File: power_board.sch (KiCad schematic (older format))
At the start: 18 parts, among them J1 STANDBY SWITCH, J2 TRANSFORMER IN, J3 BIAS OUT, J4 HEATER

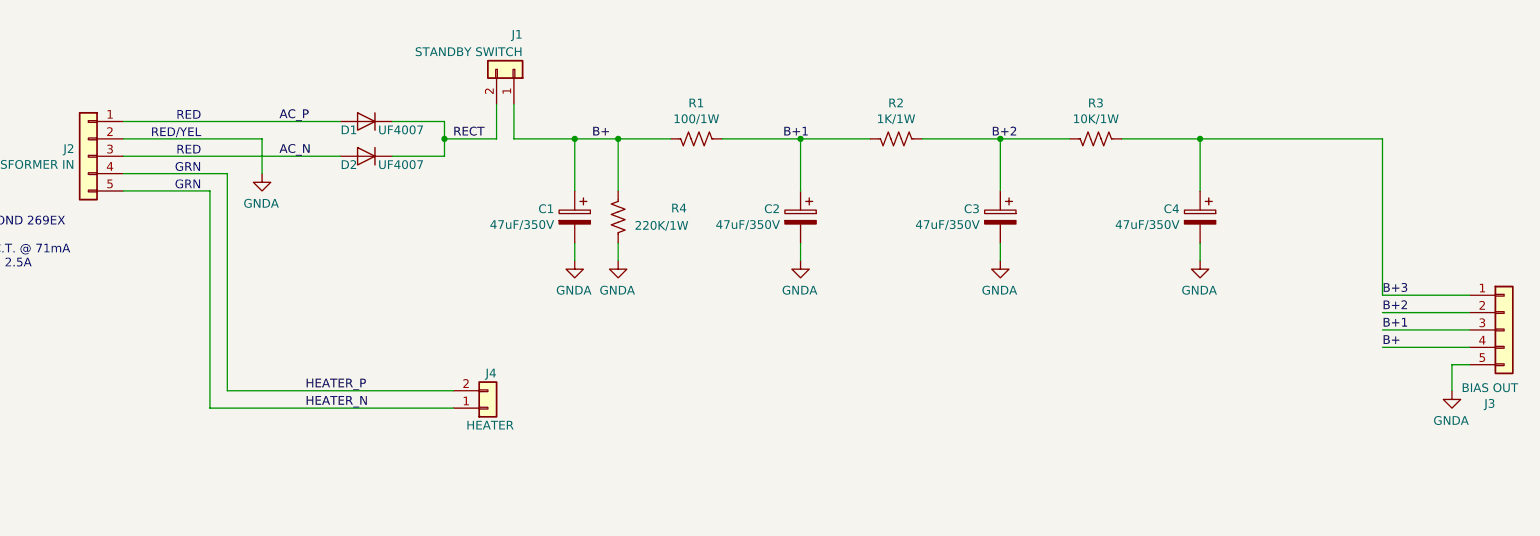
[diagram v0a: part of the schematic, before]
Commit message: rev 0.2 updates
corrected component pitch issue on connectors for BOM, made power pcb
single sided routing, added aux origin for gerber
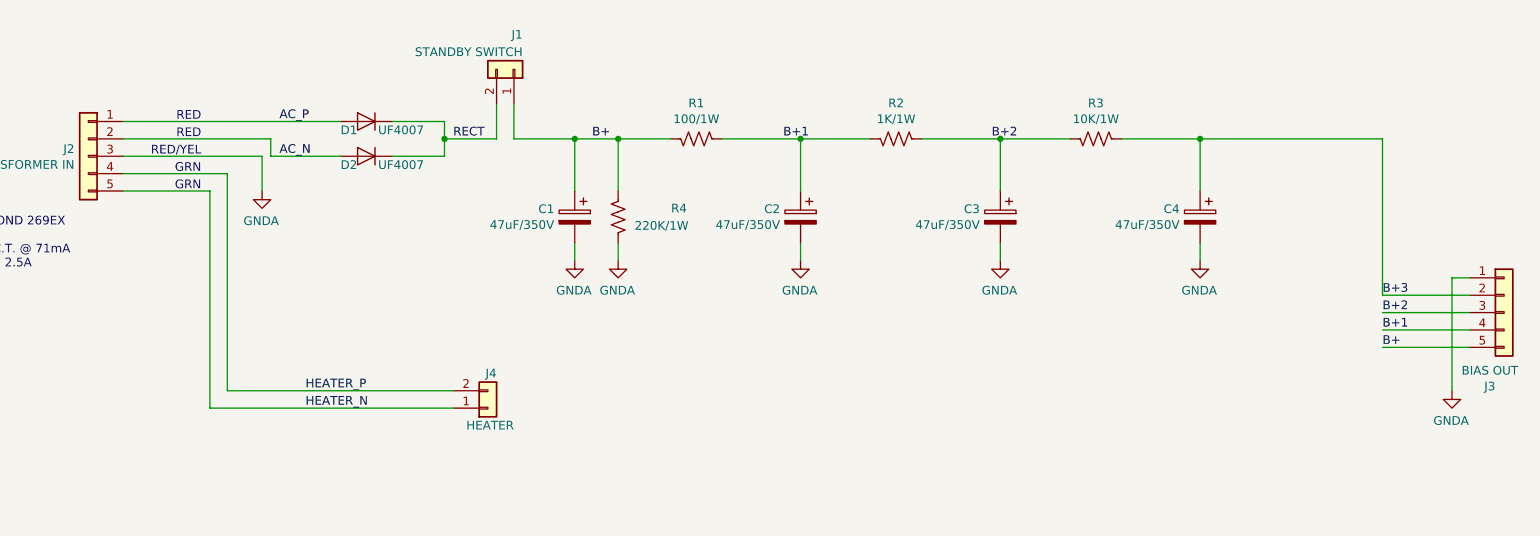
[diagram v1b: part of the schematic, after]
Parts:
- J1, J4: DIGIKEY PN 277-1721-ND -> 277-6354-ND
- J2, J3: DIGIKEY PN 277-1580-ND -> 277-7675-ND
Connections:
- net AC_N: now also J2.2 (Pin_2); no longer J2.3 (Pin_3)
- net B+: now also J3.5 (Pin_5); no longer J3.4 (Pin_4)
- net B+1: now also J3.4 (Pin_4); no longer J3.3 (Pin_3)
- net B+2: now also J3.3 (Pin_3); no longer J3.2 (Pin_2)
- net B+3: now also J3.2 (Pin_2); no longer J3.1 (Pin_1)
- net GNDA: now also J2.3 (Pin_3), J3.1 (Pin_1); no longer J2.2 (Pin_2), J3.5 (Pin_5)
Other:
- moved on the sheet: J3
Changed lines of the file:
@@
 Sheet 1 1
 Title "DUAL CHANNEL SINGLE ENDED EL84 POWER SUPPLY"
-Date "2019-05-04"
-Rev "0.1"
+Date "2019-05-19"
+Rev "0.2"
 Comp "DRAWN BY: W. SENDER"
 Comment1 "willsender@gmail.com"
@@
 F 2 "Connectors_Terminal_Blocks:TerminalBlock_Pheonix_PT-3.5mm_5pol" H 1650 2650 50  0001 C CNN
 F 3 "https://media.digikey.com/pdf/Data%20Sheets/Phoenix%20Contact%20PDFs/1935190.pdf" H 1650 2650 50  0001 C CNN
-F 4 "277-1580-ND" H 1650 2650 50  0001 C CNN "DIGIKEY PN"
+F 4 "277-7675-ND" H 1650 2650 50  0001 C CNN "DIGIKEY PN"
 	1    1650 2650
 	-1   0    0    -1
@@
 L power:GNDA #PWR01
 U 1 1 5CCDC931
-P 2650 2750
-F 0 "#PWR01" H 2650 2500 50  0001 C CNN
-F 1 "GNDA" H 2655 2577 50  0000 C CNN
-F 2 "" H 2650 2750 50  0001 C CNN
-F 3 "" H 2650 2750 50  0001 C CNN
-	1    2650 2750
+P 2650 2850
+F 0 "#PWR01" H 2650 2600 50  0001 C CNN
+F 1 "GNDA" H 2655 2677 50  0000 C CNN
+F 2 "" H 2650 2850 50  0001 C CNN
+F 3 "" H 2650 2850 50  0001 C CNN
+	1    2650 2850
 	-1   0    0    -1
 $EndComp
@@
 F 2 "Connectors_Terminal_Blocks:TerminalBlock_Pheonix_PT-3.5mm_2pol" H 4100 2150 50  0001 C CNN
 F 3 "https://media.digikey.com/pdf/Data%20Sheets/Phoenix%20Contact%20PDFs/Combicon%20Compact%20Series.pdf" H 4100 2150 50  0001 C CNN
-F 4 "277-1721-ND" H 4100 2150 50  0001 C CNN "DIGIKEY PN"
+F 4 "277-6354-ND" H 4100 2150 50  0001 C CNN "DIGIKEY PN"
 	1    4100 2150
 	0    1    -1   0
@@
 Wire Wire Line
 	3100 2450 1850 2450
-Wire Wire Line
-	3100 2650 1850 2650
 Wire Wire Line
 	1850 2750 2450 2750
@@
 Text Notes 2300 2450 2    50   ~ 0
 RED
+Text Notes 2300 2650 2    50   ~ 0
+RED/YEL
 Text Notes 2300 2550 2    50   ~ 0
-RED/YEL
-Text Notes 2300 2650 2    50   ~ 0
 RED
 Text Notes 2300 2750 2    50   ~ 0
@@
 F 2 "Connectors_Terminal_Blocks:TerminalBlock_Pheonix_PT-3.5mm_2pol" H 3950 4100 50  0001 C CNN
 F 3 "https://media.digikey.com/pdf/Data%20Sheets/Phoenix%20Contact%20PDFs/Combicon%20Compact%20Series.pdf" H 3950 4100 50  0001 C CNN
-F 4 "277-1721-ND" H 3950 4100 50  0001 C CNN "DIGIKEY PN"
+F 4 "277-6354-ND" H 3950 4100 50  0001 C CNN "DIGIKEY PN"
 	1    3950 4100
 	1    0    0    1
 $EndComp
 Wire Wire Line
-	2650 2550 1850 2550
+	2650 2650 1850 2650
 $Comp
 L Device:R_US R1
@@
 $EndComp
 Wire Wire Line
-	2650 2750 2650 2550
+	2650 2850 2650 2650
 Wire Wire Line
 	4450 2850 4450 2550
@@
 L Connector_Generic:Conn_01x05 J3
 U 1 1 5CD09EED
-P 9800 3650
-F 0 "J3" H 9718 3225 50  0000 C CNN
-F 1 "BIAS OUT" H 9718 3316 50  0000 C CNN
-F 2 "Connectors_Terminal_Blocks:TerminalBlock_Pheonix_PT-3.5mm_5pol" H 9800 3650 50  0001 C CNN
-F 3 "https://media.digikey.com/pdf/Data%20Sheets/Phoenix%20Contact%20PDFs/1935190.pdf" H 9800 3650 50  0001 C CNN
-F 4 "277-1580-ND" H 9800 3650 50  0001 C CNN "DIGIKEY PN"
-	1    9800 3650
+P 9800 3550
+F 0 "J3" H 9718 3125 50  0000 C CNN
+F 1 "BIAS OUT" H 9718 3216 50  0000 C CNN
+F 2 "Connectors_Terminal_Blocks:TerminalBlock_Pheonix_PT-3.5mm_5pol" H 9800 3550 50  0001 C CNN
+F 3 "https://media.digikey.com/pdf/Data%20Sheets/Phoenix%20Contact%20PDFs/1935190.pdf" H 9800 3550 50  0001 C CNN
+F 4 "277-7675-ND" H 9800 3550 50  0001 C CNN "DIGIKEY PN"
+	1    9800 3550
 	1    0    0    -1
 $EndComp
@@
 	-1   0    0    -1
 $EndComp
-Wire Wire Line
-	9500 4000 9500 3850
-Wire Wire Line
-	9500 3850 9600 3850
 Wire Wire Line
 	8050 2550 9100 2550
@@
 Text Label 3750 2550 0    50   ~ 0
 RECT
+Wire Wire Line
+	9500 3350 9600 3350
+Wire Wire Line
+	9500 3350 9500 4000
+Wire Wire Line
+	1850 2550 2700 2550
+Wire Wire Line
+	2700 2550 2700 2650
+Wire Wire Line
+	2700 2650 3100 2650
 $EndSCHEMATC
